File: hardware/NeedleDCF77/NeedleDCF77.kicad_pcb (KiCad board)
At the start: 2 copper layers, 130 x 30 mm, 86 parts, among them J1 USB_C_Receptacle_USB2.0, J2 Battery, J3 DSW, J4 UART, J5 Hours, J6 Minutes, J7 Seconds, Q1 AO3401A, Q2 AO3400A, SW1 ShowDate, U1 LTC3558, U2 STM32L051C8Tx, U3 MAS6180_77kHz, U4 LT1617, U5 PT6312, U6 LM4871, Y2 32.768kHz

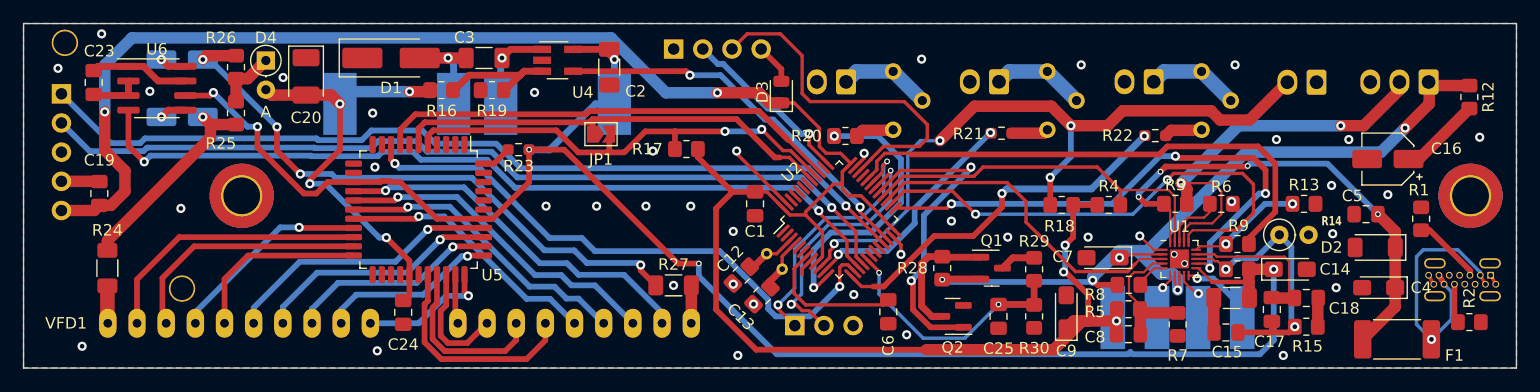
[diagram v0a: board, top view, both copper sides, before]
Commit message: Add test points to schematic and board
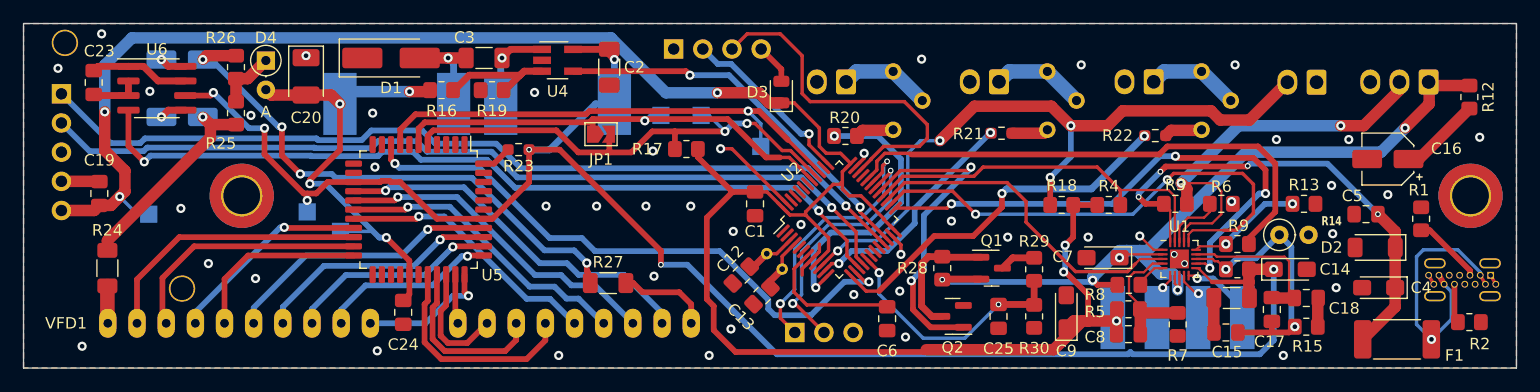
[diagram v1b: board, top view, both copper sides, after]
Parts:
- added TP1: +3V, TestPoint:TestPoint_Pad_1.5x1.5mm, B.Cu at (54.9, 115.6)
- added TP2: +5V, TestPoint:TestPoint_Pad_1.5x1.5mm, B.Cu at (68.7, 115.4)
- added TP4: MISO, TestPoint:TestPoint_Pad_1.5x1.5mm, B.Cu at (103.0, 107.0)
- added TP5: MOSI, TestPoint:TestPoint_Pad_1.5x1.5mm, B.Cu at (99.5, 107.0)
- added TP6: -24V, TestPoint:TestPoint_Pad_1.5x1.5mm, B.Cu at (71.6, 117.1)
- added TP7: SCK, TestPoint:TestPoint_Pad_1.5x1.5mm, B.Cu at (108.2, 109.7)
- moved R27 5.70 mm to (94.9, 121.6)
- moved C6 0.61 mm to (119.2, 124.7)
- moved J4 0.60 mm to (111.2, 125.9)
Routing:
- net +3V0: track 185.7 -> 191.3 mm, vias 5 -> 6
- net Net-(C22-Pad2): track 52.1 -> 47.0 mm
- net AC2: track 3.30 -> 8.33 mm
- net -24V: track 38.4 -> 42.0 mm
- net SPI1_SCK: track 40.7 -> 44.2 mm, vias 0 -> 1
- net SPI1_MISO: track 41.2 -> 44.3 mm
- net GND: track 28.4 -> 31.3 mm, vias 43 -> 48
- net +5VD: track 147.5 -> 149.4 mm, vias 6 -> 7
- net SPI1_MOSI: track 39.4 -> 41.0 mm, vias 0 -> 1
- net SPI1_NSS: track 50.9 -> 51.8 mm
- net Net-(U2-NRST): track 12.6 -> 11.9 mm

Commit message: Minor improvements regarding coupling and silkscreen
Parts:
- added C10: 100nF, Capacitor_SMD:C_0805_2012Metric_Pad1.18x1.45mm_HandSolder, F.Cu at (87.2, 117.0)
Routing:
- net +5VD: track 149.4 -> 151.8 mm
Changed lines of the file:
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@@
     (property "ki_keywords" "cap capacitor")
     (attr smd)
-    (fp_text reference "C7" (at 3.5 0.09) (layer "F.SilkS")
+    (fp_text reference "C7" (at 0 1.79) (layer "F.SilkS")
         (effects (font (size 1 1) (thickness 0.15)))
     )
@@
     (property "ki_keywords" "R resistor")
     (attr smd)
-    (fp_text reference "R21" (at -2.9 0.055) (layer "F.SilkS")
+    (fp_text reference "R21" (at -0.06 -1.55) (layer "F.SilkS")
         (effects (font (size 1 1) (thickness 0.15)))
     )
@@
     (property "ki_keywords" "R resistor")
     (attr smd)
-    (fp_text reference "R22" (at -3.29 -0.01) (layer "F.SilkS")
+    (fp_text reference "R22" (at -0.05 -1.46) (layer "F.SilkS")
         (effects (font (size 1 1) (thickness 0.15)))
     )
@@
     )
   )
+  (footprint "Capacitor_SMD:C_0805_2012Metric_Pad1.18x1.45mm_HandSolder" (layer "F.Cu")
+    (at 87.2 117 90)
+    (descr "Capacitor SMD 0805 (2012 Metric), square (rectangular) end terminal, IPC_7351 nominal with elongated pad for handsoldering. (Body size source: IPC-SM-782 page 76, https://www.pcb-3d.com/wordpress/wp-content/uploads/ipc-sm-782a_amendment_1_and_2.pdf, https://docs.google.com/spreadsheets/d/1BsfQQcO9C6DZCsRaXUlFlo91Tg2WpOkGARC1WS5S8t0/edit?usp=sharing), generated with kicad-footprint-generator")
+    (tags "capacitor handsolder")
+    (property "Kelco" "#7463")
+    (property "Sheetfile" "NeedleDCF77.kicad_sch")
+    (property "Sheetname" "")
+    (property "ki_description" "Unpolarized capacitor, small symbol")
+    (property "ki_keywords" "capacitor cap")
+    (attr smd)
+    (fp_text reference "C10" (at 0 2.6 180) (layer "F.SilkS")
+        (effects (font (size 1 1) (thickness 0.15)))
+    )
+    (fp_text value "100nF" (at 0 1.68 90) (layer "F.Fab")
+        (effects (font (size 1 1) (thickness 0.15)))
+    )
+    (fp_text user "${REFERENCE}" (at 0 0 90) (layer "F.Fab")
+        (effects (font (size 0.5 0.5) (thickness 0.08)))
+    )
+    (fp_line (start -0.261252 -0.735) (end 0.261252 -0.735)
+      (stroke (width 0.12) (type solid)) (layer "F.SilkS"))
+    (fp_line (start -0.261252 0.735) (end 0.261252 0.735)
+      (stroke (width 0.12) (type solid)) (layer "F.SilkS"))
+    (fp_line (start -1.88 -0.98) (end 1.88 -0.98)
+      (stroke (width 0.05) (type solid)) (layer "F.CrtYd"))
+    (fp_line (start -1.88 0.98) (end -1.88 -0.98)
+      (stroke (width 0.05) (type solid)) (layer "F.CrtYd"))
+    (fp_line (start 1.88 -0.98) (end 1.88 0.98)
+      (stroke (width 0.05) (type solid)) (layer "F.CrtYd"))
+    (fp_line (start 1.88 0.98) (end -1.88 0.98)
+      (stroke (width 0.05) (type solid)) (layer "F.CrtYd"))
+    (fp_line (start -1 -0.625) (end 1 -0.625)
+      (stroke (width 0.1) (type solid)) (layer "F.Fab"))
+    (fp_line (start -1 0.625) (end -1 -0.625)
+      (stroke (width 0.1) (type solid)) (layer "F.Fab"))
+    (fp_line (start 1 -0.625) (end 1 0.625)
+      (stroke (width 0.1) (type solid)) (layer "F.Fab"))
+    (fp_line (start 1 0.625) (end -1 0.625)
+      (stroke (width 0.1) (type solid)) (layer "F.Fab"))
+    (pad "1" smd roundrect (at -1.0375 0 90) (size 1.175 1.45) (layers "F.Cu" "F.Paste" "F.Mask") (roundrect_rratio 0.212766)
+      (net 2 "GND") (pintype "passive"))
+    (pad "2" smd roundrect (at 1.0375 0 90) (size 1.175 1.45) (layers "F.Cu" "F.Paste" "F.Mask") (roundrect_rratio 0.212766)
+      (net 3 "+5VD") (pintype "passive"))
+    (model "${KICAD6_3DMODEL_DIR}/Capacitor_SMD.3dshapes/C_0805_2012Metric.wrl"
+      (offset (xyz 0 0 0))
+      (scale (xyz 1 1 1))
+      (rotate (xyz 0 0 0))
+    )
+  )
   (footprint "Resistor_SMD:R_0805_2012Metric_Pad1.20x1.40mm_HandSolder" (layer "F.Cu")
     (at 115.57 108.79)
@@
   (segment (start 94.57 101.25) (end 91.85 101.25) (width 0.6) (layer "F.Cu") (net 3))
   (segment (start 84.83085 116) (end 88.0225 112.80835) (width 0.5) (layer "F.Cu") (net 3))
+  (segment (start 84.86835 115.9625) (end 84.83085 116) (width 0.5) (layer "F.Cu") (net 3))
   (segment (start 60.27 105.27) (end 60.53 105.01) (width 0.5) (layer "F.Cu") (net 3))
   (segment (start 80 116) (end 84.0625 116) (width 0.5) (layer "F.Cu") (net 3))
@@
   (segment (start 95.45 102.13) (end 94.57 101.25) (width 0.6) (layer "F.Cu") (net 3))
   (segment (start 75.073466 112.8) (end 75.172966 112.7005) (width 0.5) (layer "F.Cu") (net 3))
+  (segment (start 87.2 115.9625) (end 84.86835 115.9625) (width 0.5) (layer "F.Cu") (net 3))
   (segment (start 70.49 112.8) (end 72.7375 112.8) (width 0.5) (layer "F.Cu") (net 3))
   (segment (start 146.28995 120.3) (end 147.48995 121.5) (width 0.2) (layer "F.Cu") (net 3))

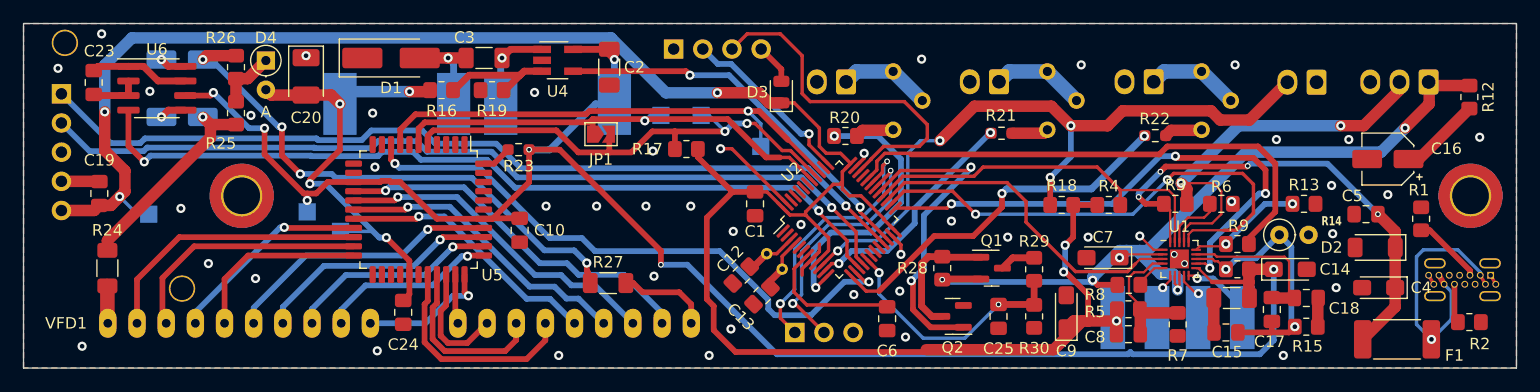
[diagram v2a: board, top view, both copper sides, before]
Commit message: Fix points from Nikola's review + add logo
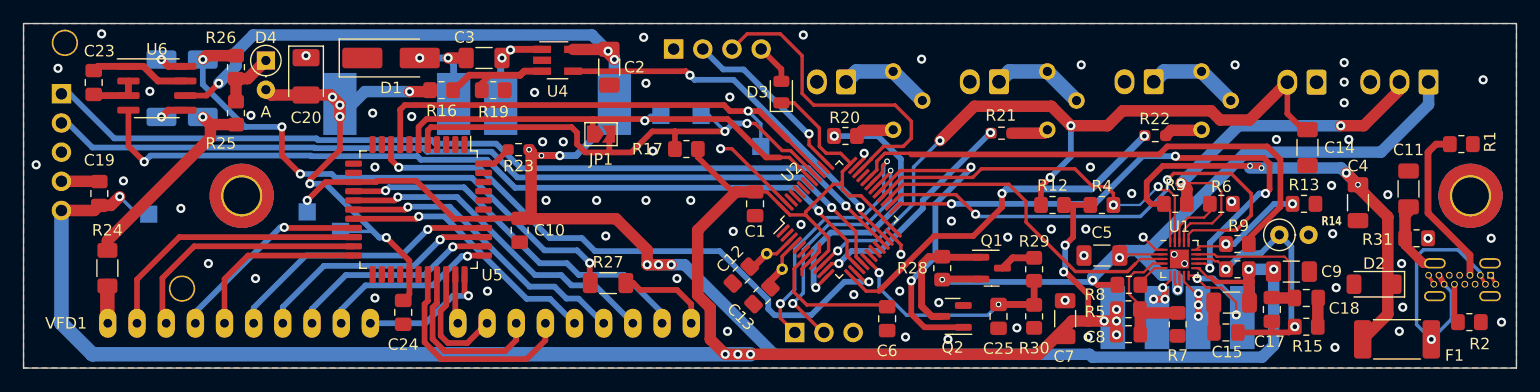
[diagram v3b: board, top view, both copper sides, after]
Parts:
- removed C16: 4.7uF, Capacitor_SMD:CP_Elec_4x5.7
- removed R18: 10k, Resistor_SMD:R_0805_2012Metric_Pad1.20x1.40mm_HandSolder
- added C11: 4.7nF, Capacitor_SMD:C_1206_3216Metric_Pad1.33x1.80mm_HandSolder, F.Cu at (164.6, 113.4)
- added G***: LOGO, Logo:Logo, B.Cu at (161.9, 123.6)
- added R31: 1M, Resistor_SMD:R_0805_2012Metric_Pad1.20x1.40mm_HandSolder, F.Cu at (165.3, 117.7)
- C14: value 10uF -> 1nF; footprint Capacitor_Tantalum_SMD:CP_EIA-3216-18_Kemet-A_Pad1.58x1.35mm_HandSolder -> Capacitor_SMD:C_1206_3216Metric_Pad1.33x1.80mm_HandSolder
- C4, C7, C9: footprint Capacitor_Tantalum_SMD:CP_EIA-3216-18_Kemet-A_Pad1.58x1.35mm_HandSolder -> Capacitor_SMD:C_1206_3216Metric_Pad1.33x1.80mm_HandSolder
- C5: value 100nF -> 10uF; footprint Capacitor_SMD:C_0805_2012Metric_Pad1.18x1.45mm_HandSolder -> Capacitor_SMD:C_1206_3216Metric_Pad1.33x1.80mm_HandSolder
- R11: value 300k -> 270k
- R12: value 1 -> 100k
- R14: value 62k -> 68k
- R3: value Rntc -> 100k
- TP2: value +5V -> +4V
- moved R12 37.5 mm to (133.6, 114.8), turned to 180 degrees
- moved C5 23.3 mm to (137.9, 119.2), turned to 180 degrees
- moved C9 19.9 mm to (154.4, 120.6), turned to 0 degrees
- moved C14 10.7 mm to (155.8, 109.8), turned to -90 degrees
- moved C4 7.62 mm to (160.2, 114.6), turned to -90 degrees
- moved R1 7.38 mm to (169.2, 109.5), turned to 0 degrees
- moved C7 6.25 mm to (134.7, 124.7), turned to 90 degrees
- moved D2 3.20 mm to (161.6, 121.7)
- moved R4 0.60 mm to (137.9, 114.8)
- moved R10 0.40 mm to (149.2, 123.3)
- moved R19 0.10 mm to (84.9, 104.8), turned to 0 degrees
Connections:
- C10 pad 2: +5VD -> +4V
- C14 pad 1: +5VD -> GPIO_EXTI0
- C2 pad 1: +5VD -> +4V
- C5 pad 1: GND -> VBAT
- C5 pad 2: VBUS_P -> GND
- C7 pad 1: VBAT -> +3V0
- C9 pad 1: +3V0 -> +4V
- J1 pad S1: GND -> Net-(J1-SHIELD)
- L1 pad 1: +5VD -> +4V
- R10 pad 1: +5VD -> +4V
- R11 pad 1: +5VD -> +4V
- R12 pad 1: VBAT -> +3V0
- R12 pad 2: Net-(C16-Pad1) -> GPIO_EXTI0
- R23 pad 1: +5VD -> +4V
- TP2 pad 1: +5VD -> +4V
- U1 pad 11: +5VD -> +4V
- U4 pad 5: +5VD -> +4V
- U5 pad 14: +5VD -> +4V
- U5 pad 38: +5VD -> +4V
- U6 pad 6: +5VD -> +4V
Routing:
- net +4V: track 0.00 -> 181.3 mm, vias 0 -> 12
- net +5VD: track 151.8 -> 0.00 mm, vias 7 -> 0
- net Net-(J1-CC1): track 6.12 -> 14.4 mm
- net Net-(C16-Pad1): track 7.12 -> 0.00 mm
- net Net-(J1-SHIELD): track 0.00 -> 6.74 mm
- net Net-(U1-SWCD2): track 6.70 -> 12.0 mm, vias 1 -> 2
- net GPIO_EXTI0: track 60.0 -> 64.4 mm
- net VBAT: track 72.9 -> 69.7 mm, vias 5 -> 4
- net SWDIO: track 31.1 -> 28.5 mm
- net +3V0: track 191.3 -> 189.1 mm, vias 6 -> 10
- net Net-(U1-SW1): track 1.32 -> 3.40 mm, vias 1 -> 3
- net Net-(U1-SWAB2): track 2.21 -> 4.20 mm, vias 1 -> 3
- net BATT_LEVEL: track 21.9 -> 19.9 mm
- net VBUS_P: track 42.8 -> 44.3 mm
- net Net-(C22-Pad2): track 47.0 -> 48.5 mm
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
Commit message: Final improvements
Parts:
- added TP3: NRST, TestPoint:TestPoint_Pad_1.5x1.5mm, B.Cu at (119.4, 124.5)
- J3: value DSW -> SWD
- moved C6 0.40 mm to (119.2, 125.1)
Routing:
- net AC2: track 8.33 -> 7.80 mm
- net Net-(U2-NRST): track 11.9 -> 12.4 mm, vias 0 -> 1
